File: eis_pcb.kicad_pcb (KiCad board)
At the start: 4 copper layers, 33 x 41 mm, 49 parts, among them J1 Conn_01x01_Socket, J12 104031-0811, J13 10051922-1810ELF, J2 GSB1C41110SSHR, J3 Conn_01x01_Socket, J7 Conn_01x02_Socket, Q3 IRLML6344TRPBF, U1 AD5941BCPZ, U2 ESP32-S3-WROOM-1U-N16R8, U4 MCP73831T-2DCI_OT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

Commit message: Draft 2
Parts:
- moved C21 5.39 mm to (129.9, 123.9)
- moved R14 5.39 mm to (118.0, 124.6)
- moved C20 5.39 mm to (129.9, 124.9)
- moved J13 5.39 mm to (125.7, 120.8)
- moved Q3 5.39 mm to (120.3, 125.2)
- moved R16 5.39 mm to (123.0, 124.3)
- moved R2 5.39 mm to (117.3, 126.5)
- moved C5 2.77 mm to (111.0, 102.1)
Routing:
- net GND: track 57.9 -> 87.6 mm, vias 34 -> 53
- net /ESP.PWM: track 28.2 -> 0.00 mm, vias 1 -> 0
- net /CTP_SDA: track 30.6 -> 41.8 mm
- net +3V3: track 26.8 -> 37.6 mm, vias 6 -> 12
- net /SCREEN.RST: track 20.0 -> 26.7 mm, vias 2 -> 3
- net /CTP_SCL: track 34.7 -> 41.3 mm
- net /MOSI: track 60.5 -> 66.6 mm
- net /CS.SCREEN: track 35.3 -> 41.4 mm
- net /SCLK: track 54.2 -> 60.4 mm
- net /CTP_RST: track 21.0 -> 26.5 mm
- net /DC: track 21.0 -> 25.7 mm, vias 2 -> 1
- net /CTP_INT: track 13.5 -> 17.5 mm
- net /REF.1V8: track 1.22 -> 3.98 mm
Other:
- board size 33 x 41 mm -> 33 x 41.2 mm

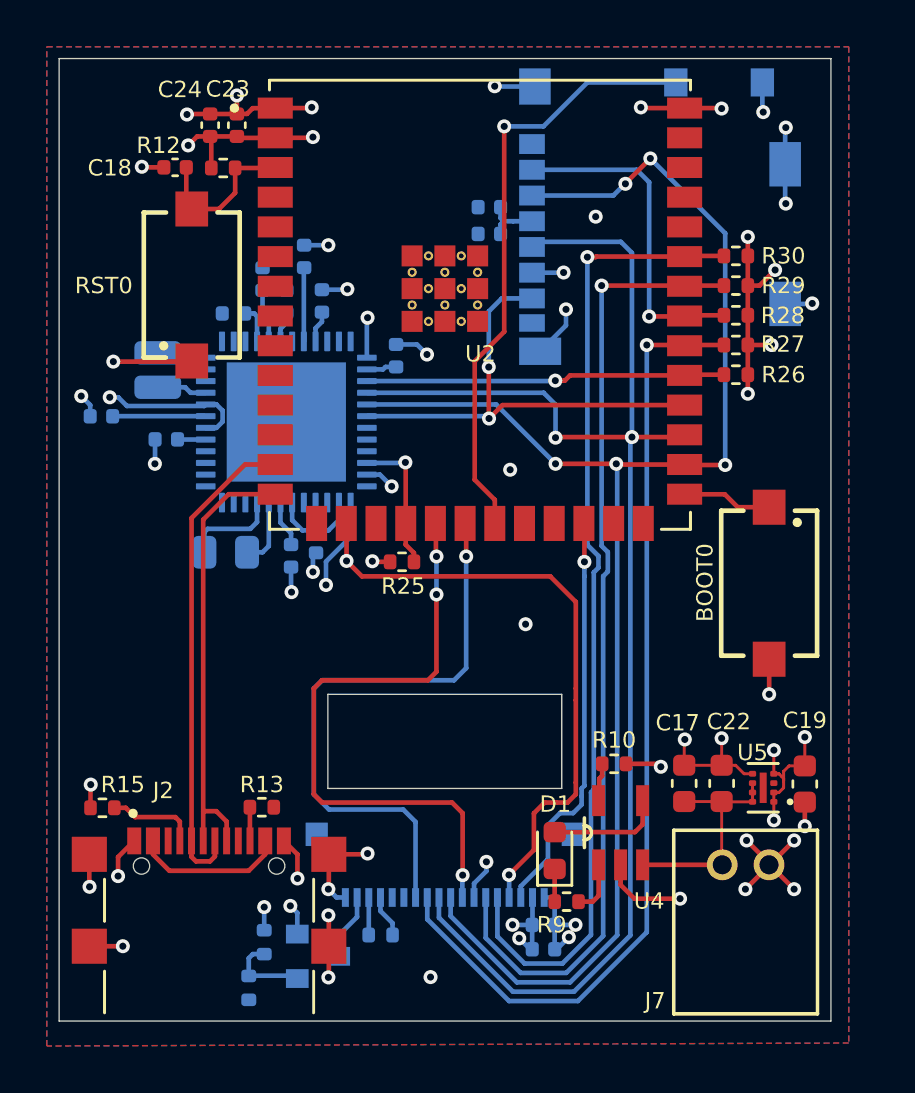
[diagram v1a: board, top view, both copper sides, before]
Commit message: Updated to esp+antenna
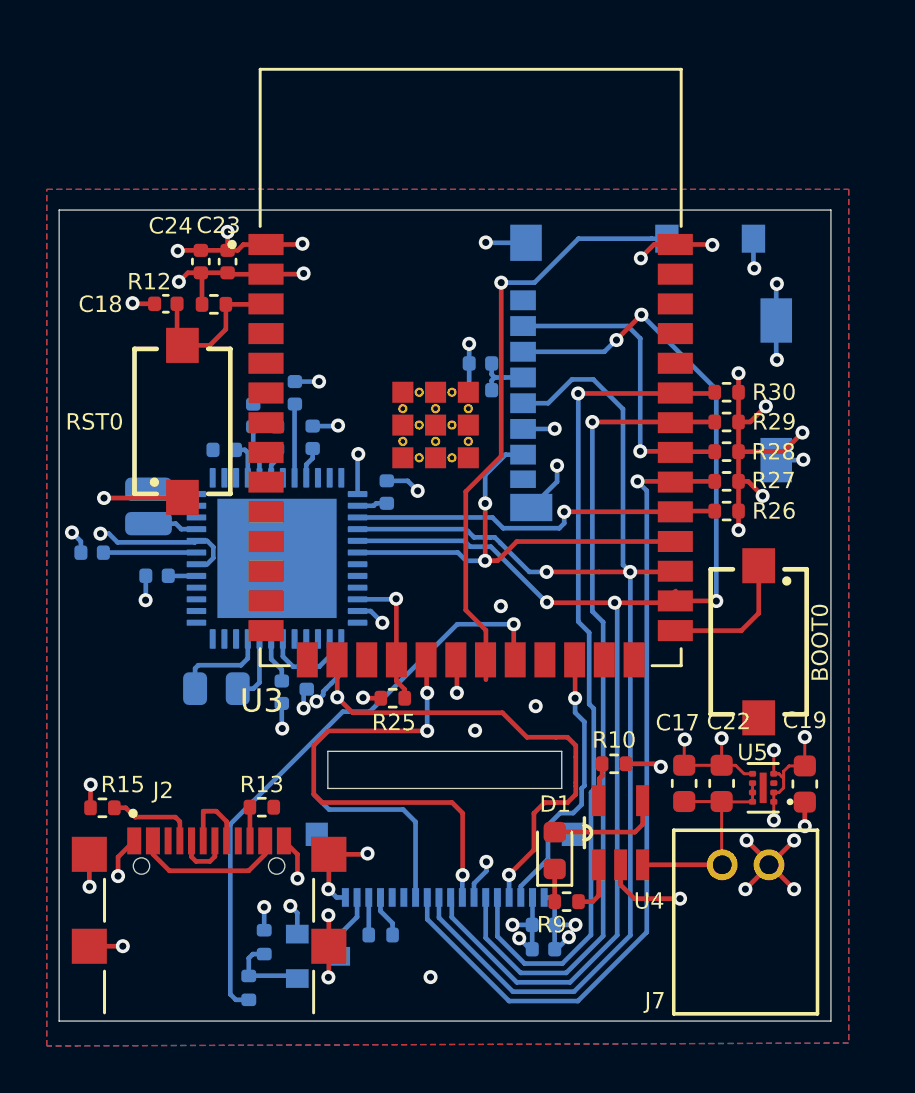
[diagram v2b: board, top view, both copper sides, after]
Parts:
- removed U2: ESP32-S3-WROOM-1U-N16R8, ESP32_S3_WROOM_1U_N16R8:XCVR_ESP32-S3-WROOM-1U-N16R8
- added U3: ESP32-S3-WROOM-1-N8R8, ESP32-S3-WROOM-1-N8R8:XCVR_ESP32S3WROOM1N8R8, F.Cu at (126.8, 100.0)
- moved C12 6.69 mm to (127.3, 99.8)
- moved C11 6.69 mm to (127.3, 101.0)
- moved J12 6.69 mm to (134.5, 100.3)
- moved C1 5.84 mm to (118.6, 103.0)
- moved C10 5.84 mm to (120.1, 103.0)
- moved C18 5.84 mm to (113.8, 97.3)
- moved C2 5.84 mm to (119.8, 113.3)
- moved C4 5.84 mm to (123.3, 105.3)
- moved C5 5.84 mm to (110.7, 107.9)
- moved C6 5.84 mm to (116.3, 103.5)
- moved C7 5.84 mm to (118.8, 113.9)
- moved C8 5.84 mm to (117.5, 102.1)
- moved J1 5.84 mm to (113.1, 105.2)
- moved J3 5.84 mm to (113.1, 106.7)
- moved R1 5.84 mm to (116.0, 113.8)
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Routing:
- net /ESP.PWM: track 0.00 -> 25.4 mm, vias 0 -> 1
- net /DATA-: track 20.8 -> 2.52 mm
- net /DC: track 25.7 -> 9.50 mm
- net /DATA+: track 19.3 -> 3.28 mm
- net /MOSI: track 66.6 -> 60.1 mm
- net /SCLK: track 60.4 -> 53.9 mm
- net /SCREEN.RST: track 26.7 -> 20.6 mm
- net /CTP_SDA: track 41.8 -> 36.0 mm
- net /CTP_SCL: track 41.3 -> 35.4 mm
- net /CTP_INT: track 17.5 -> 11.8 mm
- net /CS.SCREEN: track 41.4 -> 35.7 mm
- net /CTP_RST: track 26.5 -> 20.9 mm
- net GND: track 87.6 -> 83.7 mm, vias 53 -> 51
- net +3V3: track 37.6 -> 40.9 mm, vias 12 -> 13
- net unconnected-(U3-GND-Pad1)_9: track 0.00 -> 3.33 mm, vias 0 -> 2
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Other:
- board size 33 x 41.2 mm -> 33 x 34.7 mm

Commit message: Fixed wiring issues
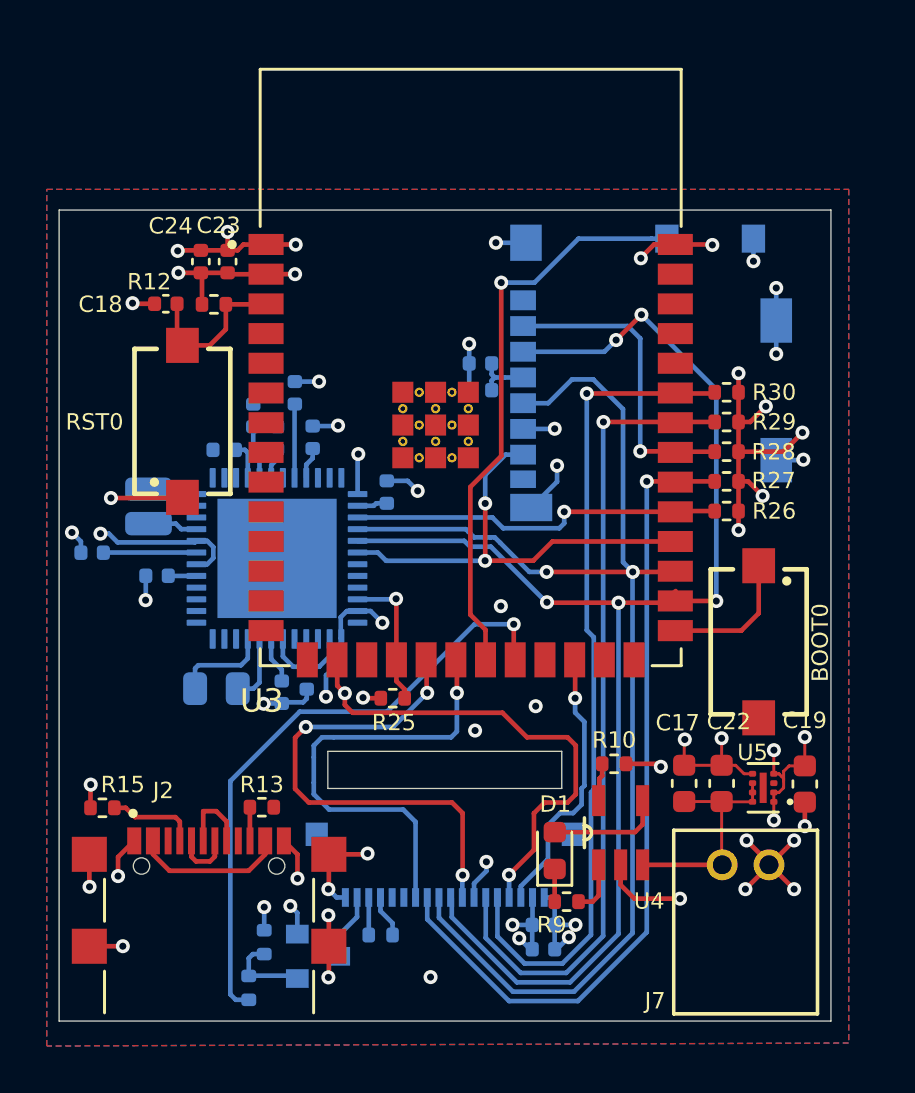
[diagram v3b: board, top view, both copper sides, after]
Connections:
- U3 pad 1: unconnected-(U3-GND-Pad1) -> GND
- U3 pad 40: unconnected-(U3-GND-Pad1)_9 -> GND
- U3 pad 41_1: unconnected-(U3-GND-Pad1)_1 -> GND
- U3 pad 41_2: unconnected-(U3-GND-Pad1)_8 -> GND
- U3 pad 41_3: unconnected-(U3-GND-Pad1)_7 -> GND
- U3 pad 41_4: unconnected-(U3-GND-Pad1)_10 -> GND
- U3 pad 41_5: unconnected-(U3-GND-Pad1)_3 -> GND
- U3 pad 41_6: unconnected-(U3-GND-Pad1)_5 -> GND
- U3 pad 41_7: unconnected-(U3-GND-Pad1)_6 -> GND
- U3 pad 41_8: unconnected-(U3-GND-Pad1)_4 -> GND
- U3 pad 41_9: unconnected-(U3-GND-Pad1)_2 -> GND
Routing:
- net /DC: track 9.50 -> 19.6 mm
- net unconnected-(U3-GND-Pad1)_9: track 3.33 -> 0.00 mm, vias 2 -> 0
- net GND: track 83.7 -> 87.1 mm, vias 51 -> 52
- net /ESP.PWM: track 25.4 -> 26.4 mm
- net /SW1: track 25.8 -> 24.8 mm
- net /SCREEN.RST: track 20.6 -> 21.3 mm
- net /CTP_SCL: track 35.4 -> 34.8 mm
- net /CS.SCREEN: track 35.7 -> 35.2 mm
- net /CTP_SDA: track 36.0 -> 35.5 mm
- net +3V3: track 40.9 -> 40.4 mm

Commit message: Stable version
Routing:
- net GND: track 87.1 -> 91.2 mm, vias 52 -> 57
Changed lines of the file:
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@@
 	)
 	(segment
+		(start 118.416364 118.8224)
+		(end 119.1756 118.8224)
+		(width 0.2)
+		(layer "F.Cu")
+		(net 1)
+	)
+	(segment
 		(start 134.112 95.3262)
 		(end 134.6768 94.7614)
@@
 	)
 	(segment
+		(start 119.1756 118.8224)
+		(end 119.2022 118.7958)
+		(width 0.2)
+		(layer "F.Cu")
+		(net 1)
+	)
+	(segment
 		(start 114.486 105.6026)
 		(end 114.5126 105.576)
@@
 	)
 	(via
+		(at 123.4694 121.4374)
+		(size 0.6)
+		(drill 0.3)
+		(layers "F.Cu" "B.Cu")
+		(net 1)
+	)
+	(via
+		(at 119.2022 118.7958)
+		(size 0.6)
+		(drill 0.3)
+		(layers "F.Cu" "B.Cu")
+		(net 1)
+	)
+	(via
 		(at 111.4552 105.6026)
 		(size 0.6)
@@
 	)
 	(via
+		(at 135.9662 120.2436)
+		(size 0.6)
+		(drill 0.3)
+		(layers "F.Cu" "B.Cu")
+		(free yes)
+		(net 1)
+	)
+	(via
 		(at 120.7516 126.098802)
 		(size 0.6)
@@
 	)
 	(via
-		(at 128.127 110.2254)
+		(at 124.587 124.5108)
+		(size 0.6)
+		(drill 0.3)
+		(layers "F.Cu" "B.Cu")
+		(net 1)
+	)
+	(via
+		(at 128.3716 109.7026)
+		(size 0.6)
+		(drill 0.3)
+		(layers "F.Cu" "B.Cu")
+		(free yes)
+		(net 1)
+	)
+	(via
+		(at 130.7592 111.0742)
 		(size 0.6)
 		(drill 0.3)
@@
 	)
 	(segment
+		(start 124.587 123.8504)
+		(end 124.587 124.5108)
+		(width 0.2)
+		(layer "B.Cu")
+		(net 1)
+	)
+	(segment
 		(start 121.2806 111.603)
 		(end 121.2806 110.697458)
@@
 	)
 	(segment
+		(start 123.48 121.448)
+		(end 123.4694 121.4374)
+		(width 0.2)
+		(layer "B.Cu")
+		(net 1)
+	)
+	(segment
+		(start 123.48 122.682)
+		(end 123.48 121.448)
+		(width 0.2)
+		(layer "B.Cu")
+		(net 1)
+	)
+	(segment
 		(start 119.8266 113.7763)
 		(end 119.8266 114.1836)
@@
 	)
 	(segment
+		(start 123.98 123.2434)
+		(end 124.587 123.8504)
+		(width 0.2)
+		(layer "B.Cu")
+		(net 1)
+	)
+	(segment
 		(start 131.3138 123.8546)
 		(end 131.318 123.8504)
@@
 	)
 	(segment
+		(start 123.98 122.682)
+		(end 123.98 123.2434)
+		(width 0.2)
+		(layer "B.Cu")
+		(net 1)
+	)
+	(segment
 		(start 139.9012 99.441)
 		(end 139.9012 98.0138)
@@
 	)
 	(segment
+		(start 122.284 114.1624)
+		(end 122.9942 114.1624)
+		(width 0.2)
+		(layer "F.Cu")
+		(net 10)
+	)
+	(segment
 		(start 119.3292 96.0314)
 		(end 118.086 96.0314)
@@
 	)
 	(segment
-		(start 122.9942 114.1624)
-		(end 122.2596 114.1624)
-		(width 0.2)
-		(layer "F.Cu")
-		(net 10)
-	)
-	(segment
 		(start 118.0658 96.0356)
 		(end 116.5052 96.0356)
@@
 	)
 	(segment
-		(start 122.2596 114.1624)
-		(end 122.2342 114.137)
-		(width 0.2)
-		(layer "F.Cu")
-		(net 10)
-	)
-	(segment
 		(start 138.289 103.6214)
 		(end 138.289 102.3514)
@@
 	)
 	(segment
+		(start 122.2596 114.138)
+		(end 122.284 114.1624)
+		(width 0.2)
+		(layer "F.Cu")
+		(net 10)
+	)
+	(segment
 		(start 140.2167 117.2885)
 		(end 140.4496 117.0556)
@@
 	)
 	(via
-		(at 122.2342 114.137)
+		(at 122.2596 114.138)
 		(size 0.6)
 		(drill 0.3)
@@
 	)
 	(segment
-		(start 121.455688 113.952815)
-		(end 121.455688 114.448502)
+		(start 121.361498 113.731048)
+		(end 121.233921 113.731048)
 		(width 0.2)
 		(layer "F.Cu")
@@
 	)
 	(segment
-		(start 130.978942 118.6216)
-		(end 130.0008 118.6216)
+		(start 131.331 118.269542)
+		(end 130.978942 118.6216)
 		(width 0.2)
 		(layer "F.Cu")
@@
 	)
 	(segment
-		(start 131.331 118.269542)
-		(end 130.978942 118.6216)
+		(start 130.978942 118.6216)
+		(end 130.0008 118.6216)
 		(width 0.2)
 		(layer "F.Cu")
@@
 	)
 	(segment
-		(start 129.54 120.65)
-		(end 128.4732 121.7168)
+		(start 121.361498 113.731048)
+		(end 121.455688 113.825238)
 		(width 0.2)
 		(layer "F.Cu")
@@
 	)
 	(segment
-		(start 121.131586 113.628713)
-		(end 121.131586 112.531986)
+		(start 129.2438 115.8326)
+		(end 130.978942 115.8326)
 		(width 0.2)
 		(layer "F.Cu")
@@
 	)
 	(segment
-		(start 121.455688 113.952815)
+		(start 121.790586 114.7834)
+		(end 128.1946 114.7834)
+		(width 0.2)
+		(layer "F.Cu")
+		(net 38)
+	)
+	(segment
+		(start 121.233921 113.731048)
 		(end 121.131586 113.628713)
 		(width 0.2)
@@
 	)
 	(segment
-		(start 128.1946 114.7834)
-		(end 129.2438 115.8326)
+		(start 121.455688 113.825238)
+		(end 121.455688 114.448502)
 		(width 0.2)
 		(layer "F.Cu")
@@
 	)
 	(segment
-		(start 129.54 119.0824)
-		(end 129.54 120.65)
+		(start 130.978942 115.8326)
+		(end 131.331 116.184658)
 		(width 0.2)
 		(layer "F.Cu")
@@
 	)
 	(segment
-		(start 130.0008 118.6216)
-		(end 129.54 119.0824)
+		(start 128.1946 114.7834)
+		(end 129.2438 115.8326)
 		(width 0.2)
 		(layer "F.Cu")
@@
 	)
 	(segment
-		(start 130.978942 115.8326)
-		(end 131.331 116.184658)
+		(start 129.54 119.0824)
+		(end 129.54 120.65)
 		(width 0.2)
 		(layer "F.Cu")
@@
 	)
 	(segment
-		(start 129.2438 115.8326)
-		(end 130.978942 115.8326)
+		(start 129.54 120.65)
+		(end 128.4732 121.7168)
 		(width 0.2)
 		(layer "F.Cu")
@@
 	)
 	(segment
-		(start 121.790586 114.7834)
-		(end 128.1946 114.7834)
+		(start 121.131586 113.628713)
+		(end 121.131586 112.531986)
+		(width 0.2)
+		(layer "F.Cu")
+		(net 38)
+	)
+	(segment
+		(start 130.0008 118.6216)
+		(end 129.54 119.0824)
 		(width 0.2)
 		(layer "F.Cu")
@@
 	)
 	(via
-		(at 121.455688 113.952815)
+		(at 121.361498 113.731048)
 		(size 0.6)
 		(drill 0.3)

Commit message: Improved wiring
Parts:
- moved R13 0.36 mm to (117.9, 118.5)
- moved D1 0.18 mm to (130.6, 120.7)
- moved R9 0.16 mm to (131.1, 122.8)
- moved U4 0.08 mm to (133.3, 119.9)
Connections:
- U3 pad 15: unconnected-(U3-IO3-Pad15) -> /DC
- U3 pad 16: /CTP_RST -> /CS.SCREEN
- U3 pad 19: /SCREEN.RST -> unconnected-(U3-IO11-Pad19)
- U3 pad 20: /DC -> unconnected-(U3-IO12-Pad20)
- U3 pad 23: unconnected-(U3-IO21-Pad23) -> /SCREEN.RST
- U3 pad 24: /CTP_INT -> /CTP_RST
- U3 pad 25: unconnected-(U3-IO48-Pad25) -> /CTP_INT
- U3 pad 32: /CS.SCREEN -> unconnected-(U3-IO39-Pad32)
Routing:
- net +5V: track 11.4 -> 26.8 mm
- net /DATA-: track 2.52 -> 14.8 mm
- net /DATA+: track 3.28 -> 13.2 mm
- net /CTP_RST: track 21.0 -> 12.3 mm, vias 2 -> 1
- net /SCREEN.RST: track 21.3 -> 13.9 mm, vias 3 -> 1
- net /DC: track 19.6 -> 12.9 mm
- net GND: track 91.2 -> 90.0 mm, vias 57 -> 58
- net /CTP_INT: track 11.8 -> 12.3 mm
